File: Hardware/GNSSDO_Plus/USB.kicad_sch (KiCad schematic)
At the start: 31 parts, among them J2 USB_C_Receptacle, J4 USB_C_Receptacle, Q1 MBT3904DW1, SW1 PTH_RA_h7.5mm, SW2 PTH_RA_h7.5mm, SW3 PTH_RA_h7.5mm, U3 CH340C

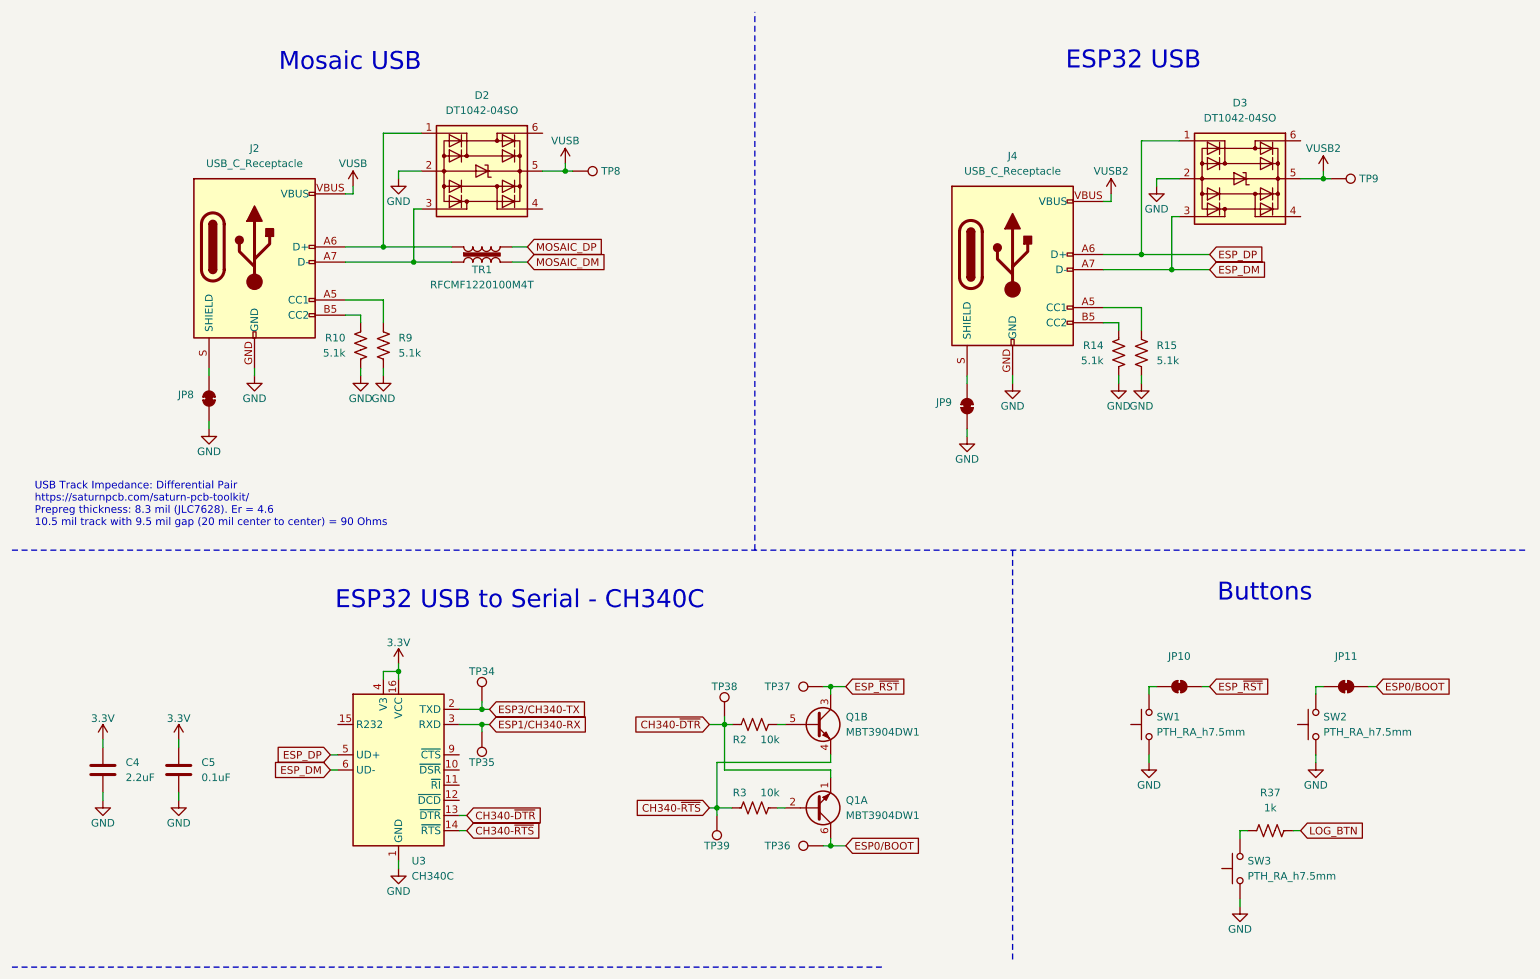
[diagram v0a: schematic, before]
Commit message: GNSSDO+ : update symbols and footprints
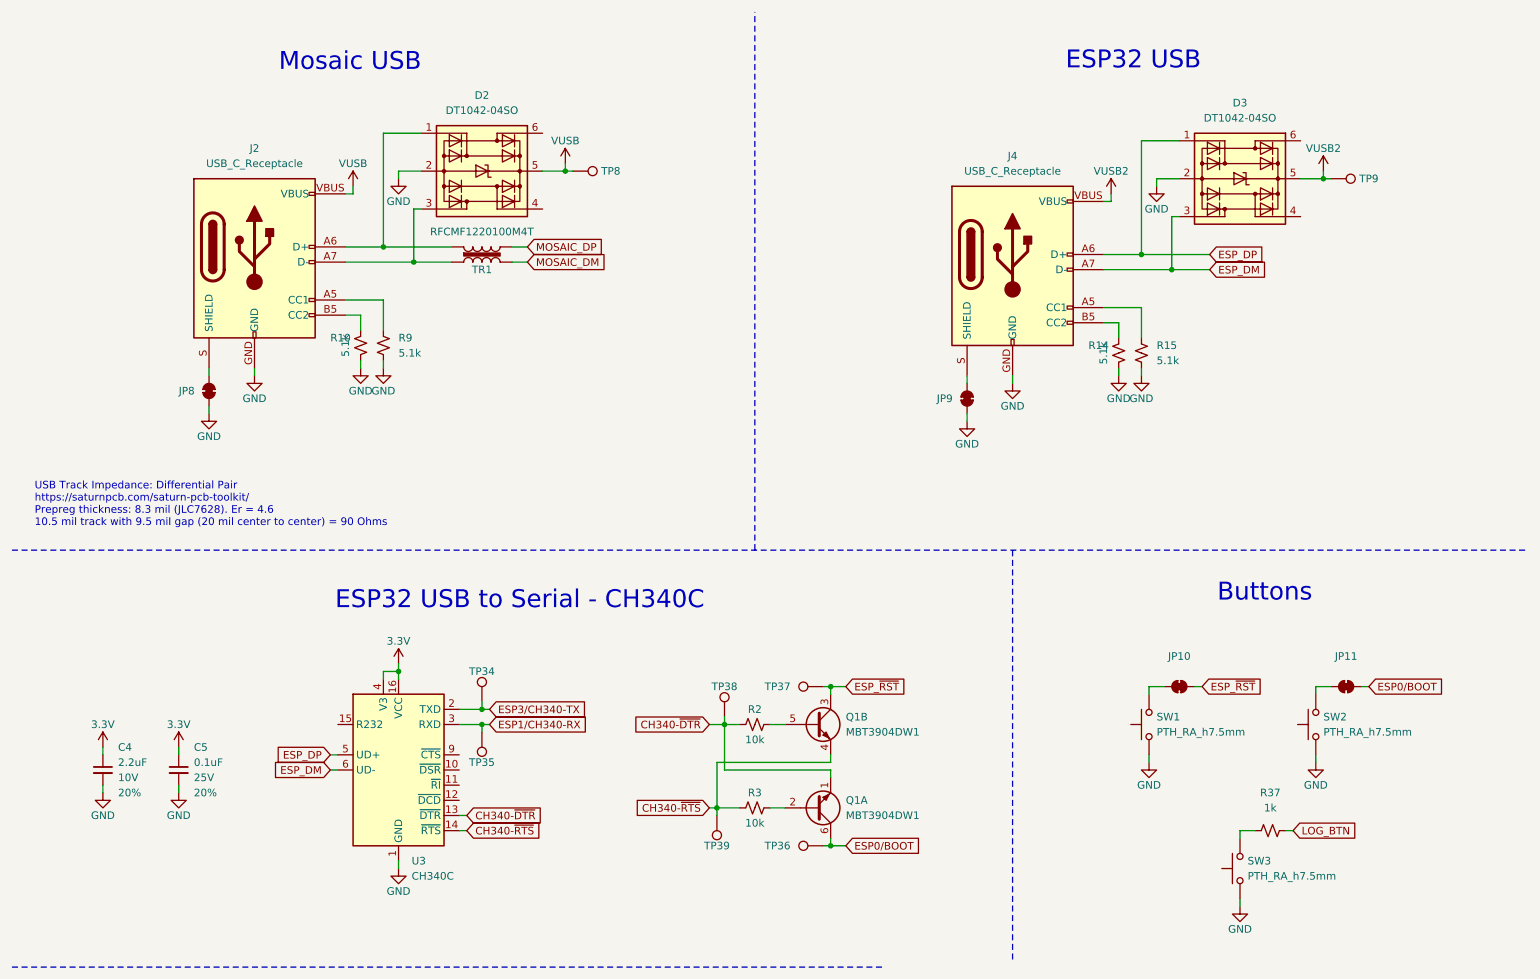
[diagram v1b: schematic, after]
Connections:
- net CH340-~{DTR}: now also R2.1; no longer R2.2
- net CH340-~{RTS}: now also R3.1; no longer R3.2
- net GND: now also R10.2, R14.2, R15.2, R9.2; no longer R10.1, R14.1, R15.1, R9.1
- net LOG_BTN: now also R37.2; no longer R37.1
- net at Q1.2 (B1): now also R3.2; no longer R3.1
- net at J4.A5 (CC1): now also R15.1; no longer R15.2
- net at J4.B5 (CC2): now also R14.1; no longer R14.2
- net at J2.B5 (CC2): now also R10.1; no longer R10.2
- net at SW3.2: now also R37.1; no longer R37.2
- net at Q1.5 (B2): now also R2.2; no longer R2.1
- net at J2.A5 (CC1): now also R9.1; no longer R9.2
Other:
- moved on the sheet: JP8, JP9

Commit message: GNSSDO Plus - ready for review
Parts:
- added JP1: ~, SparkFun-Jumper:Jumper_2_NC_Trace, symbol SparkFun-Jumper:SolderJumper_2_Bridged
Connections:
- net at SW3.2: now also JP1.1 (A); no longer R37.1
- new net: JP1.2 (B), R37.1
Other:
- moved on the sheet: JP10, JP11, R37, SW1, SW2

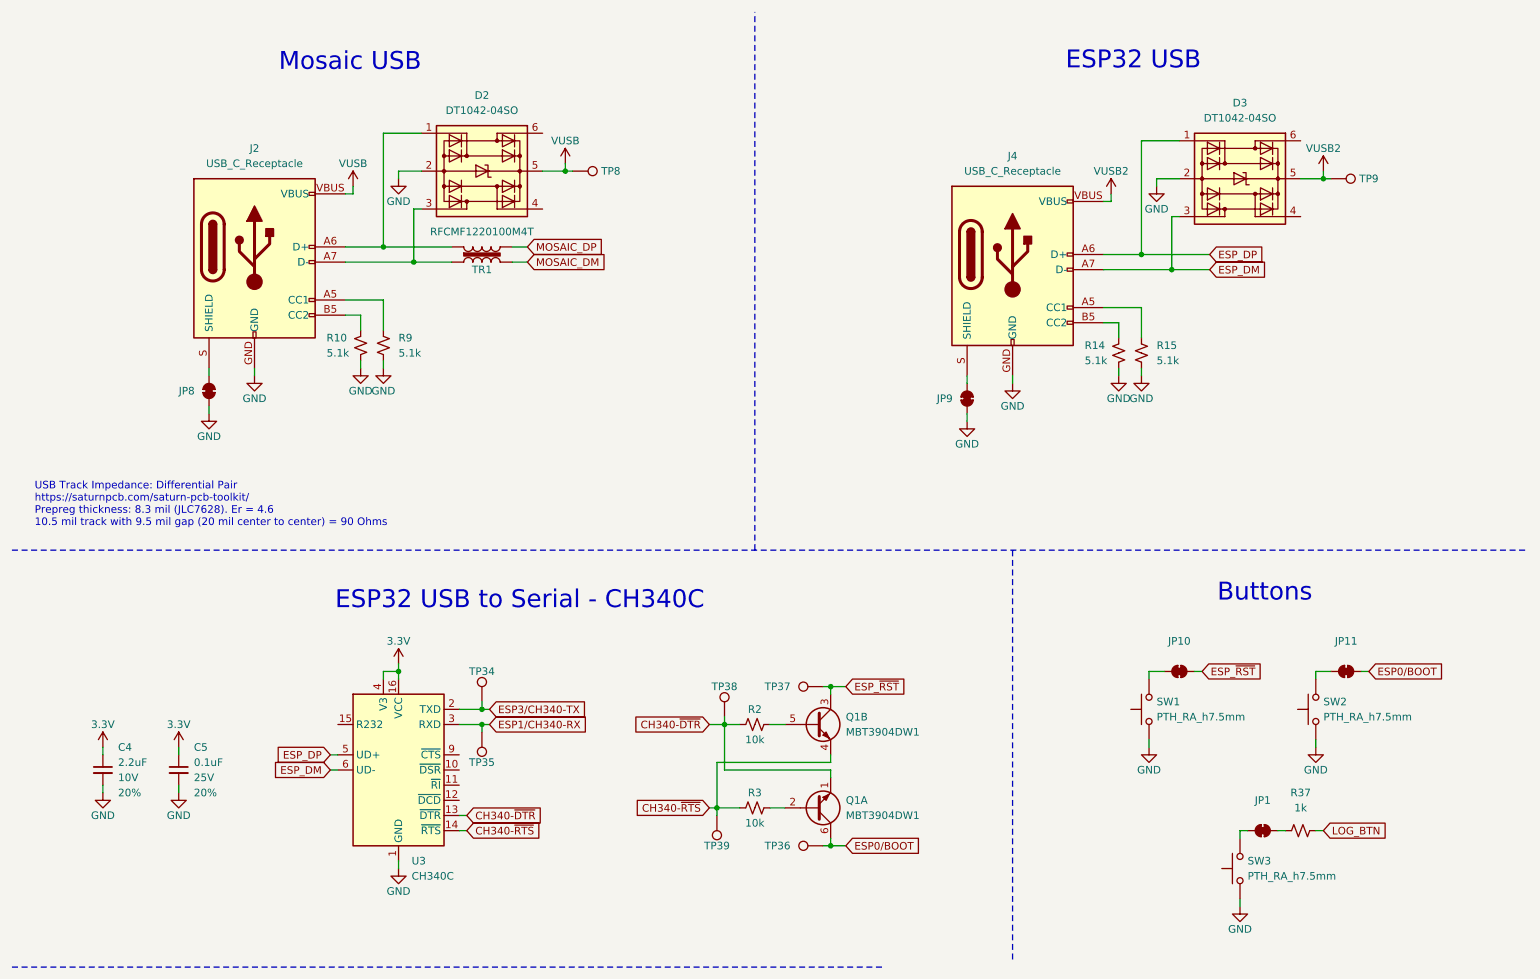
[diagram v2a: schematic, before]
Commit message: GNSSDO+ v02 PCB - with DP5305 PoE module, PowerPath Controllers and MS8607 PHT sensor
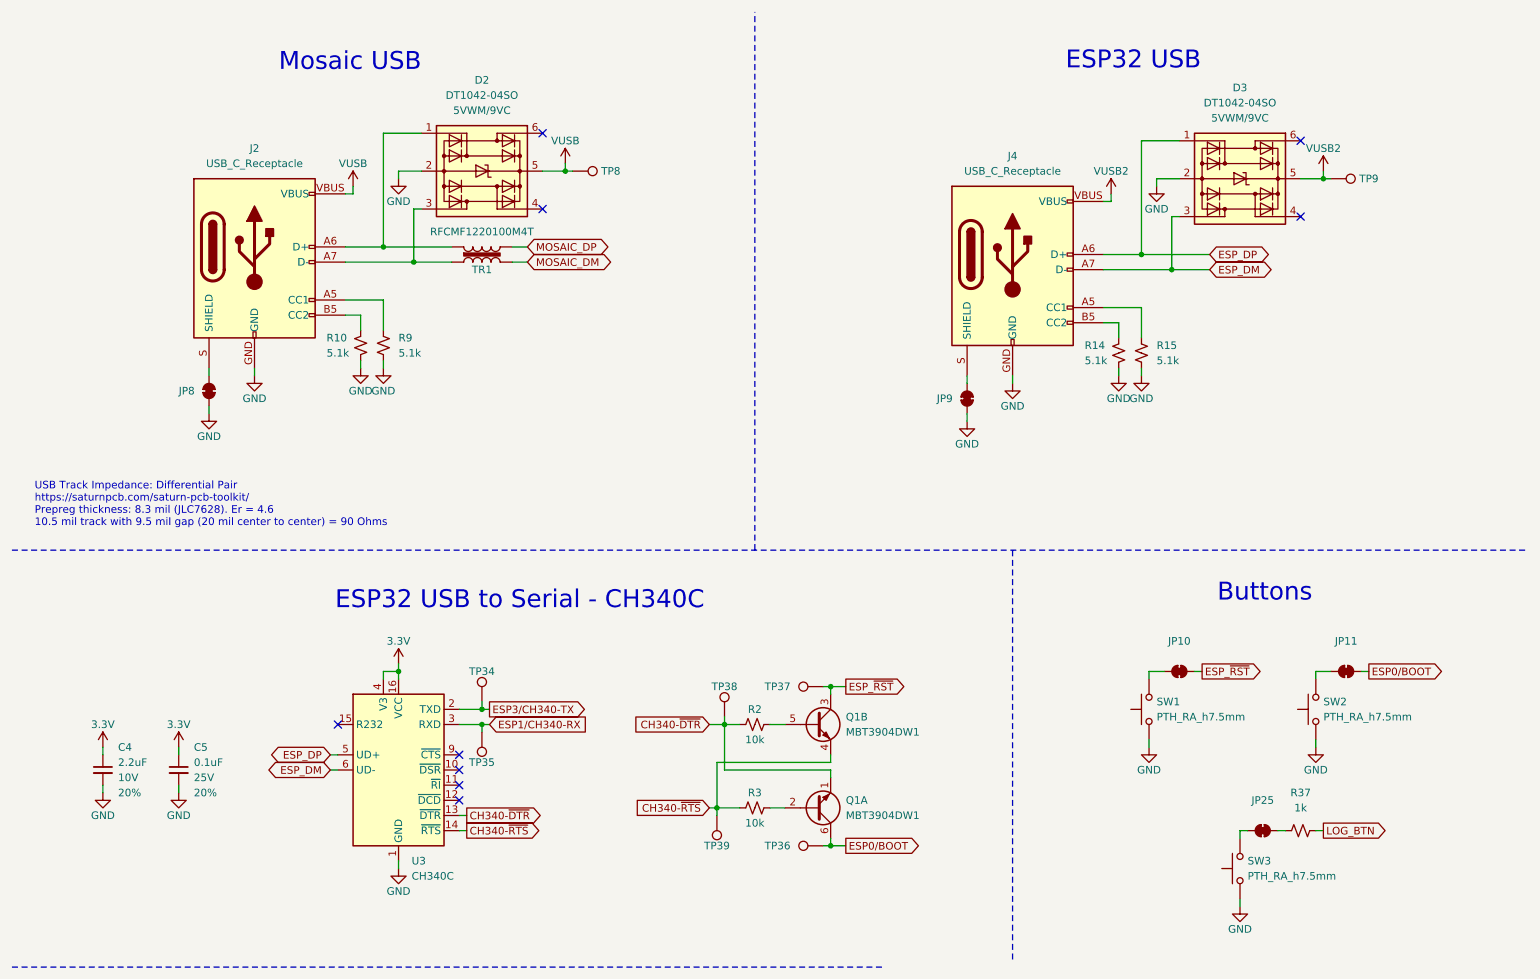
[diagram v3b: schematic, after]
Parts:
- D2, D3: symbol SparkFun-DiscreteSemi:D_TVS_ESD_USB -> SparkFun-DiscreteSemi:D_TVS_ESD_USB_5V; Rating (none) -> 5VWM/9VC
- renumbered JP1 to JP25
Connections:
- no-connect marks 0 -> 9
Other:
- title: USB -> GNSSDO Plus - USB

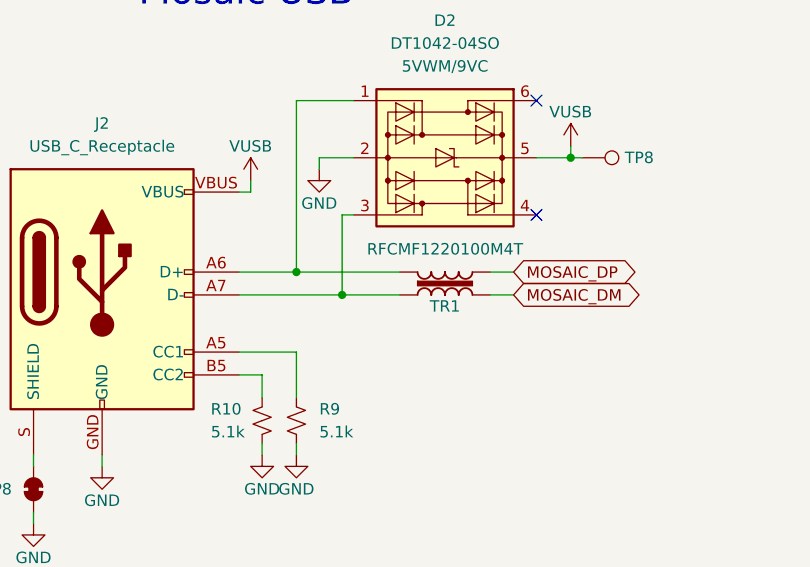
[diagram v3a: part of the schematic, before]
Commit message: Update GNSSDO KiCad files to match latest SparkFun library
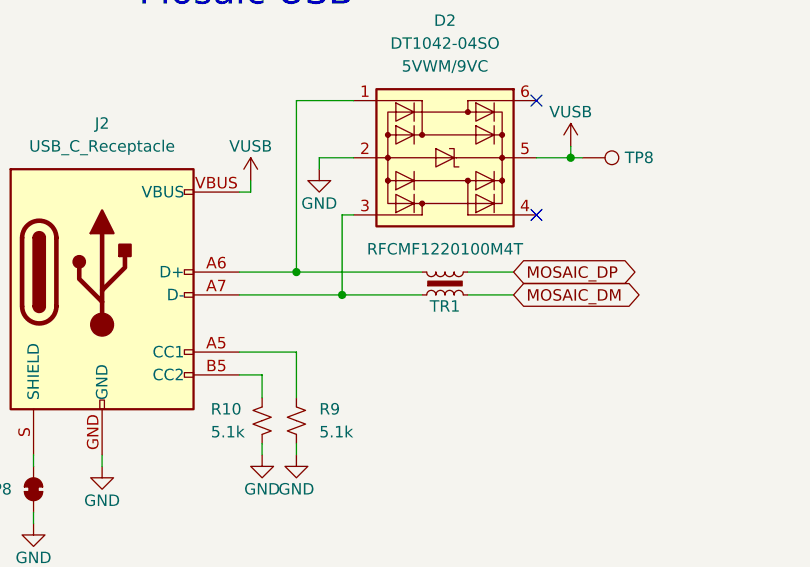
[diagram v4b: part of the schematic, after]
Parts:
- C4: PROD_ID CAP-07888 -> CAP-24999
- Q1: footprint SparkFun-Semiconductor-Standard:SOT-323 -> SparkFun-Semiconductor-Standard:SOT-363_SC-70-6
- TP34, TP35, TP36, TP37, TP38, TP39, TP8, TP9: footprint SparkFun-Connector:1x01 -> SparkFun-Connector:1x01_P2.54mm
- TR1: footprint SparkFun-Coil:RFCMF1220100M4T -> SparkFun-Coil:Choke_100MHz_USB
